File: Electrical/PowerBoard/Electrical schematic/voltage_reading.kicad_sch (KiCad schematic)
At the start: 3 parts, among them U3 TLV2370IDBVR

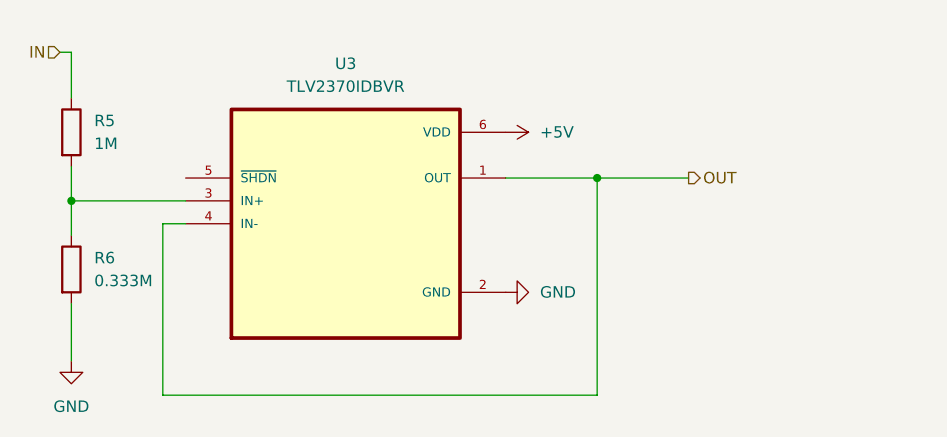
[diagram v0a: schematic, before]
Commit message: rewiring to be smaller/new mux/ fixing xt60
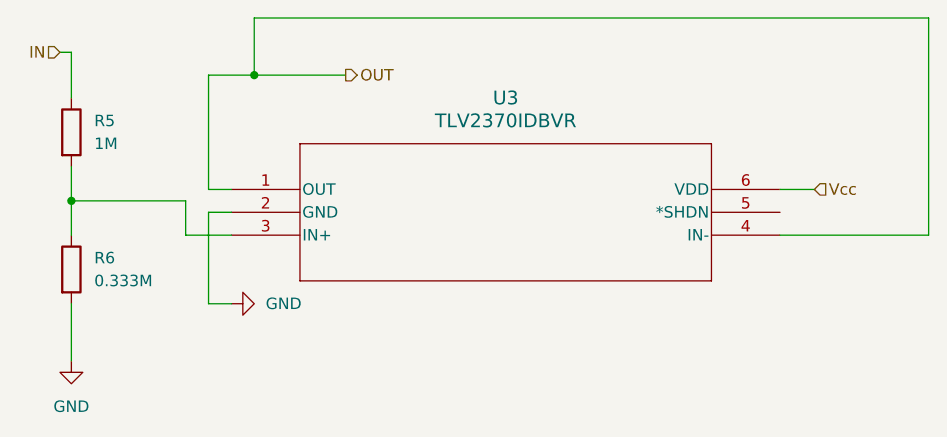
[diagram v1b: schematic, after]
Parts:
- removed U3: TLV2370IDBVR, TLV2370IDBVR:SOT95P280X145-6N, symbol TLV2370IDBVR:TLV2370IDBVR
- added U3: TLV2370IDBVR, DBV6, symbol 2025-02-22_17-10-12:TLV2370IDBVR
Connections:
- net GND: now also U3.2 (GND)
- net OUT: now also U3.1 (OUT), U3.4 (IN-)
- net at R5.2, R6.1: now also U3.3 (IN+)
- new net Vcc: U3.6 (VDD)
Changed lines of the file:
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@@
 	)
 	(junction
-		(at 167.64 93.98)
+		(at 129.54 82.55)
 		(diameter 0)
 		(color 0 0 0 0)
@@
 	(wire
 		(pts
-			(xy 119.38 99.06) (xy 121.92 99.06)
-		)
-		(stroke
-			(width 0)
-			(type default)
-		)
-	)
-	(wire
-		(pts
-			(xy 167.64 93.98) (xy 167.64 118.11)
+			(xy 127 95.25) (xy 124.46 95.25)
+		)
+		(stroke
+			(width 0)
+			(type default)
+		)
+	)
+	(wire
+		(pts
+			(xy 204.47 100.33) (xy 204.47 76.2)
+		)
+		(stroke
+			(width 0)
+			(type default)
+		)
+	)
+	(wire
+		(pts
+			(xy 124.46 95.25) (xy 124.46 82.55)
+		)
+		(stroke
+			(width 0)
+			(type default)
+		)
+	)
+	(wire
+		(pts
+			(xy 187.96 95.25) (xy 191.77 95.25)
+		)
+		(stroke
+			(width 0)
+			(type default)
+		)
+	)
+	(wire
+		(pts
+			(xy 204.47 76.2) (xy 129.54 76.2)
+		)
+		(stroke
+			(width 0)
+			(type default)
+		)
+	)
+	(wire
+		(pts
+			(xy 129.54 76.2) (xy 129.54 82.55)
 		)
 		(stroke
@@
 	(wire
 		(pts
-			(xy 167.64 93.98) (xy 177.8 93.98)
-		)
-		(stroke
-			(width 0)
-			(type default)
-		)
-	)
-	(wire
-		(pts
-			(xy 157.48 93.98) (xy 167.64 93.98)
+			(xy 187.96 100.33) (xy 204.47 100.33)
+		)
+		(stroke
+			(width 0)
+			(type default)
+		)
+	)
+	(wire
+		(pts
+			(xy 124.46 82.55) (xy 129.54 82.55)
+		)
+		(stroke
+			(width 0)
+			(type default)
+		)
+	)
+	(wire
+		(pts
+			(xy 129.54 82.55) (xy 139.7 82.55)
 		)
 		(stroke
@@
 	(wire
 		(pts
-			(xy 119.38 118.11) (xy 119.38 99.06)
+			(xy 121.92 100.33) (xy 121.92 96.52)
+		)
+		(stroke
+			(width 0)
+			(type default)
+		)
+	)
+	(wire
+		(pts
+			(xy 124.46 107.95) (xy 124.46 97.79)
+		)
+		(stroke
+			(width 0)
+			(type default)
+		)
+	)
+	(wire
+		(pts
+			(xy 124.46 97.79) (xy 127 97.79)
+		)
+		(stroke
+			(width 0)
+			(type default)
+		)
+	)
+	(wire
+		(pts
+			(xy 127 100.33) (xy 121.92 100.33)
 		)
 		(stroke
@@
 	(wire
 		(pts
-			(xy 119.38 118.11) (xy 167.64 118.11)
+			(xy 127 107.95) (xy 124.46 107.95)
 		)
 		(stroke
@@
 			(width 0)
 			(type default)
+		)
+	)
+	(hierarchical_label "Vcc"
+		(shape input)
+		(at 191.77 95.25 0)
+		(fields_autoplaced yes)
+		(effects
+			(font
+				(size 1.27 1.27)
+			)
+			(justify left)
 		)
 	)
@@
 	(hierarchical_label "OUT"
 		(shape output)
-		(at 177.8 93.98 0)
+		(at 139.7 82.55 0)
 		(fields_autoplaced yes)
 		(effects
@@
 	(symbol
 		(lib_id "power:GND")
-		(at 157.48 106.68 90)
+		(at 127 107.95 90)
 		(unit 1)
 		(exclude_from_sim no)
@@
 		(fields_autoplaced yes)
 		(property "Reference" "#PWR010"
-			(at 163.83 106.68 0)
+			(at 133.35 107.95 0)
 			(effects
 				(font
@@
 		)
 		(property "Value" "GND"
-			(at 161.29 106.6799 90)
+			(at 130.81 107.9499 90)
 			(effects
 				(font
@@
 		)
 		(property "Footprint" ""
-			(at 157.48 106.68 0)
+			(at 127 107.95 0)
 			(effects
 				(font
@@
 		)
 		(property "Datasheet" ""
-			(at 157.48 106.68 0)
+			(at 127 107.95 0)
 			(effects
 				(font
@@
 		)
 		(property "Description" "Power symbol creates a global label with name \"GND\" , ground"
-			(at 157.48 106.68 0)
+			(at 127 107.95 0)
 			(effects
 				(font
@@
 	)
 	(symbol
-		(lib_id "TLV2370IDBVR:TLV2370IDBVR")
-		(at 139.7 99.06 0)
+		(lib_id "2025-02-22_17-10-12:TLV2370IDBVR")
+		(at 127 95.25 0)
 		(unit 1)
 		(exclude_from_sim no)
@@
 		(fields_autoplaced yes)
 		(property "Reference" "U3"
-			(at 139.7 81.28 0)
-			(effects
-				(font
-					(size 1.27 1.27)
+			(at 157.48 85.09 0)
+			(effects
+				(font
+					(size 1.524 1.524)
 				)
 			)
 		)
 		(property "Value" "TLV2370IDBVR"
-			(at 139.7 83.82 0)
-			(effects
-				(font
-					(size 1.27 1.27)
-				)
-			)
-		)
-		(property "Footprint" "TLV2370IDBVR:SOT95P280X145-6N"
-			(at 139.7 99.06 0)
-			(effects
-				(font
-					(size 1.27 1.27)
-				)
-				(justify bottom)
-				(hide yes)
-			)
-		)
-		(property "Datasheet" ""
-			(at 139.7 99.06 0)
-			(effects
-				(font
-					(size 1.27 1.27)
+			(at 157.48 87.63 0)
+			(effects
+				(font
+					(size 1.524 1.524)
+				)
+			)
+		)
+		(property "Footprint" "DBV6"
+			(at 127 95.25 0)
+			(effects
+				(font
+					(size 1.27 1.27)
+					(italic yes)
+				)
+				(hide yes)
+			)
+		)
+		(property "Datasheet" "TLV2370IDBVR"
+			(at 127 95.25 0)
+			(effects
+				(font
+					(size 1.27 1.27)
+					(italic yes)
 				)
 				(hide yes)
@@
 		)
 		(property "Description" ""
-			(at 139.7 99.06 0)
-			(effects
-				(font
-					(size 1.27 1.27)
-				)
-				(hide yes)
-			)
+			(at 127 95.25 0)
+			(effects
+				(font
+					(size 1.27 1.27)
+				)
+				(hide yes)
+			)
+		)
+		(pin "2"
 		)
 		(pin "5"
 		)
+		(pin "3"
+		)
+		(pin "1"
+		)
 		(pin "6"
-		)
-		(pin "3"
-		)
-		(pin "2"
-		)
-		(pin "1"
 		)
 		(pin "4"
@@
 					(unit 1)
 				)
-			)
-		)
-	)
-	(symbol
-		(lib_id "power:+5V")
-		(at 157.48 88.9 270)
-		(unit 1)
-		(exclude_from_sim no)
-		(in_bom yes)
-		(on_board yes)
-		(dnp no)
-		(fields_autoplaced yes)
-		(property "Reference" "#PWR012"
-			(at 153.67 88.9 0)
-			(effects
-				(font
-					(size 1.27 1.27)
-				)
-				(hide yes)
-			)
-		)
-		(property "Value" "+5V"
-			(at 161.29 88.8999 90)
-			(effects
-				(font
-					(size 1.27 1.27)
-				)
-				(justify left)
-			)
-		)
-		(property "Footprint" ""
-			(at 157.48 88.9 0)
-			(effects
-				(font
-					(size 1.27 1.27)
-				)
-				(hide yes)
-			)
-		)
-		(property "Datasheet" ""
-			(at 157.48 88.9 0)
-			(effects
-				(font
-					(size 1.27 1.27)
-				)
-				(hide yes)
-			)
-		)
-		(property "Description" "Power symbol creates a global label with name \"+5V\""
-			(at 157.48 88.9 0)
-			(effects
-				(font
-					(size 1.27 1.27)
-				)
-				(hide yes)
-			)
-		)
-		(pin "1"
-		)
-		(instances
-			(project ""
-				(path "/f95f296f-a4bf-4952-bdc7-66087a6cc347/3a70a2bc-721e-442a-a054-b13b147c0577"
-					(reference "#PWR012")
-					(unit 1)
-				)
